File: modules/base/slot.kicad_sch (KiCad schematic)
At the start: 8 parts, among them J7 Conn_01x02, U6 TPS2111APWR

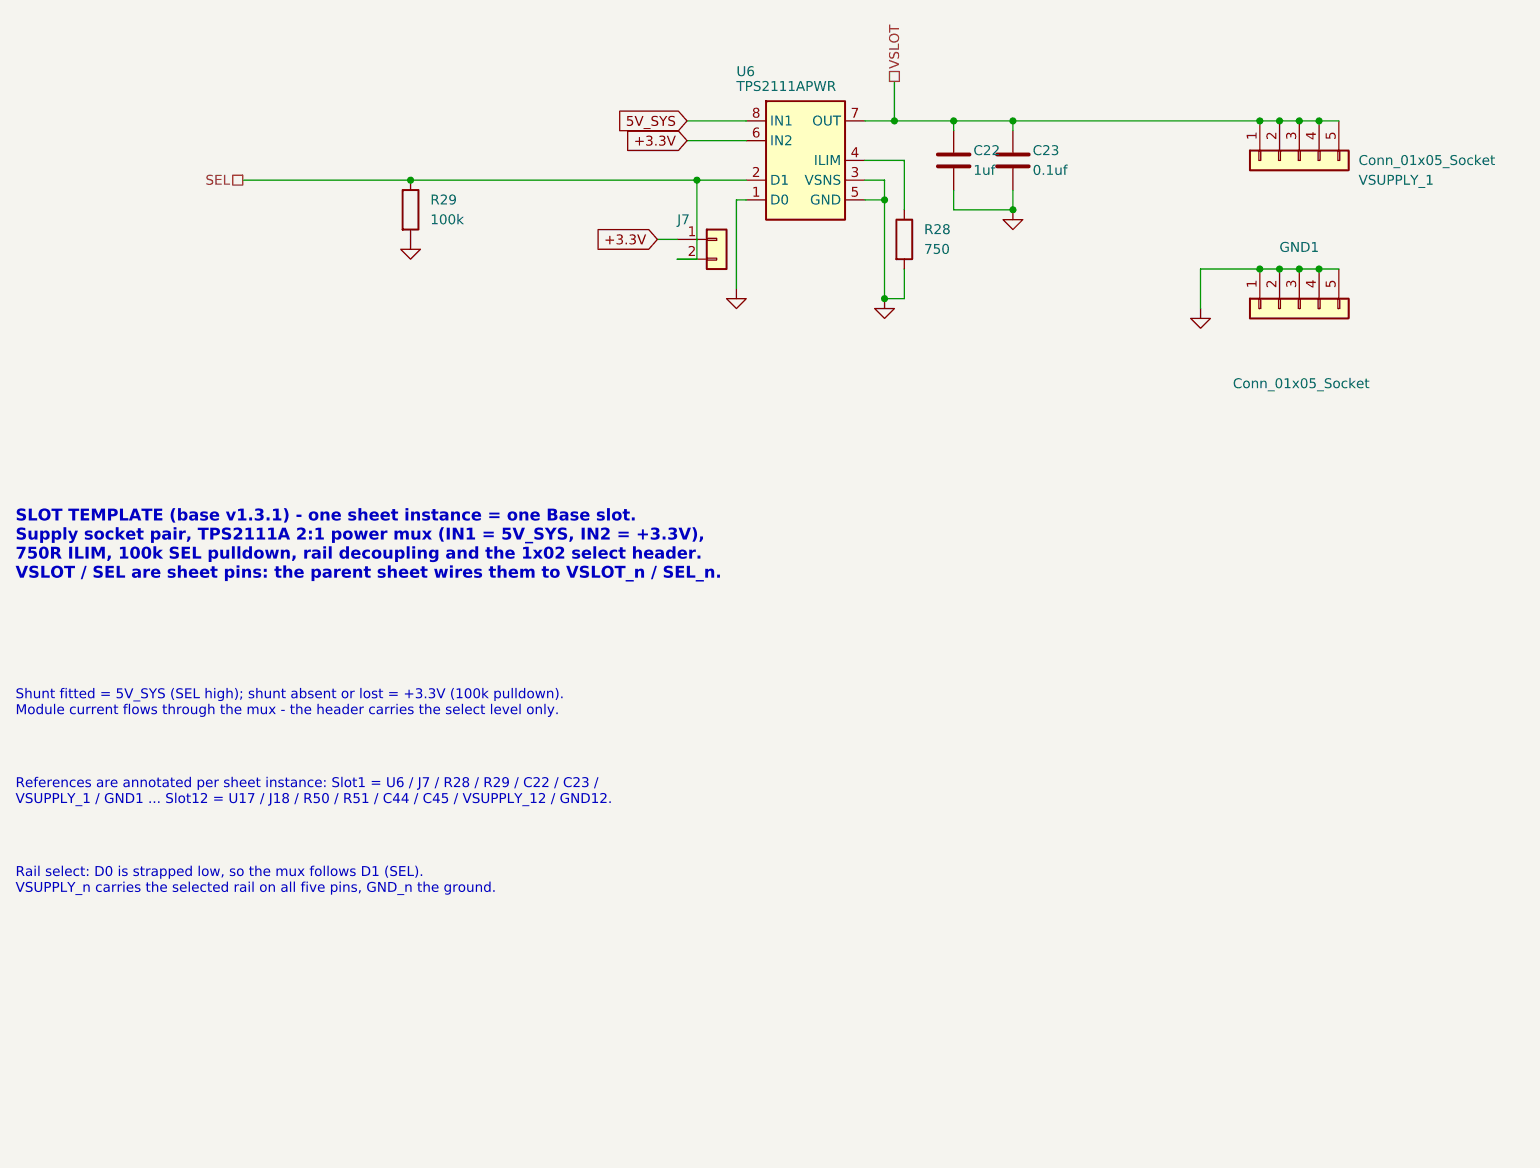
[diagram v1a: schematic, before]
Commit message: base: 1.3.8 (schematic only) - per-slot 2:1 mux swapped TPS2111APWR -> TPS2116DRLR (C3235557, ~$13/board cheaper), 12x 750R ILIM resistors deleted; docs/verification updated. NOTE: documented release blocker (reset press can drive a 3.3V-jumpered slot to 5V_SYS) + ILIM limit lost; PCB pending
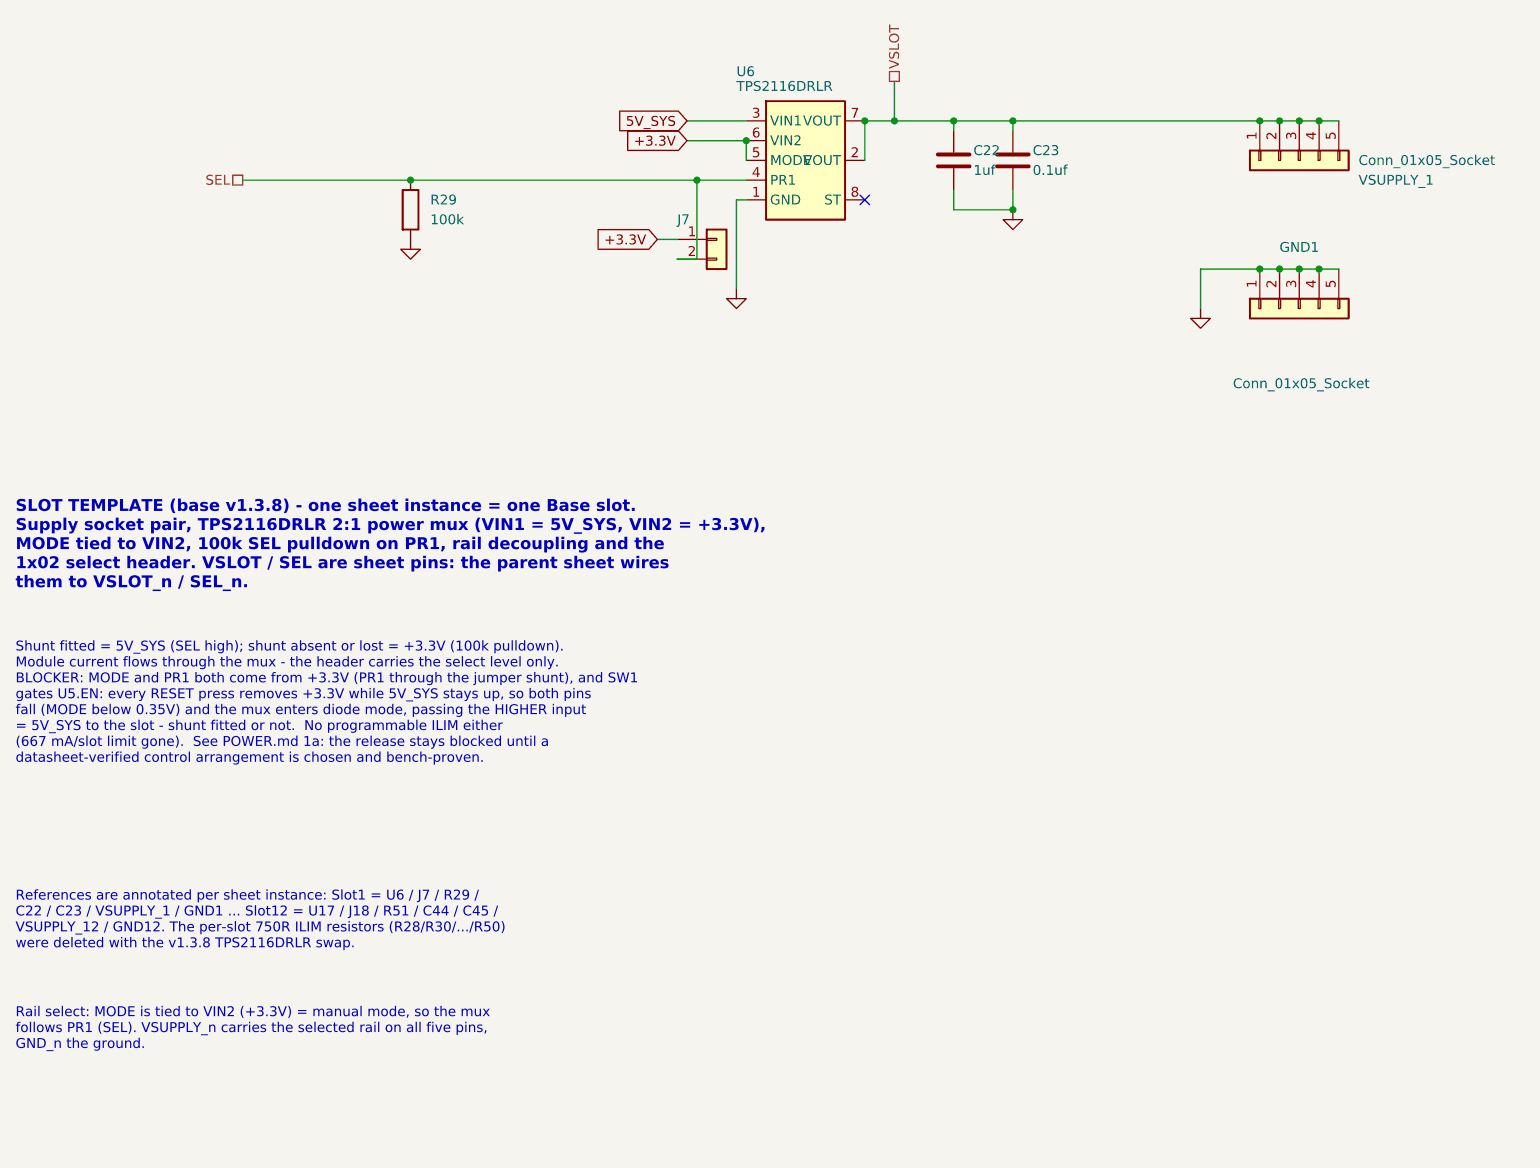
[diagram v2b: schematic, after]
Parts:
- removed R28: 750, Resistor_SMD:R_0402_1005Metric, symbol Device:R
- U6: value TPS2111APWR -> TPS2116DRLR; footprint Package_SO:TSSOP-8_4.4x3mm_P0.65mm -> Package_TO_SOT_SMD:SOT-583-8; symbol BreadModular_PowerMux:TPS2111APWR -> BreadModular_PowerMux:TPS2116DRLR; LCSC C471060 -> C3235557; MPN TPS2111APWR -> TPS2116DRLR
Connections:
- net +3.3V: now also U6.5 (MODE)
- net 5V_SYS: now also U6.3 (VIN1); no longer U6.8 (IN1)
- net GND: no longer U6.3 (VSNS), U6.5 (GND)
- net SEL: now also U6.4 (PR1); no longer U6.2 (D1)
- net VSLOT: now also U6.2 (VOUT)
- no-connect marks 0 -> 1
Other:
- note added: "Rail select: MODE is tied to VIN2 (+3.3V) = manual mode, so the mux follows PR1 (SEL). VSUPPLY_n carries the selected rail on all five pins, GND_n the ground."
- note added: "References are annotated per sheet instance: Slot1 = U6 / J7 / R29 / C22 / C23 / VSUPPLY_1 / GND1 ... Slot12 = U17 / J18 / R51 / C44 / C45 / VSUPPLY_12 / GND12. The per-slot 750R ILIM resistors (R28/R30/.../R50) were deleted with the v1.3.8 TPS2116DRLR swap."
- note added: "SLOT TEMPLATE (base v1.3.8) - one sheet instance = one Base slot. Supply socket pair, TPS2116DRLR 2:1 power mux (VIN1 = 5V_SYS, VIN2 = +3.3V), MODE tied to VIN2, 100k SEL pulldown on PR1, rail decoupling and the 1x02 select header. VSLOT / SEL are sheet pins: the parent sheet wires them to VSLOT_n / SEL_n."
- note added: "Shunt fitted = 5V_SYS (SEL high); shunt absent or lost = +3.3V (100k pulldown). Module current flows through the mux - the header carries the select level only. BLOCKER: MODE and PR1 both come from +3.3V (PR1 through the jumper shunt), and SW1 gates U5.EN: every RESET press removes +3.3V while 5V_SYS stays up, so both pins fall (MODE below 0.35V) and the mux enters diode mode, passing the HIGHER 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"
- note removed: "Rail select: D0 is strapped low, so the mux follows D1 (SEL). VSUPPLY_n carries the selected rail on all five pins, GND_n the ground."
- note removed: "References are annotated per sheet instance: Slot1 = U6 / J7 / R28 / R29 / C22 / C23 / VSUPPLY_1 / GND1 ... Slot12 = U17 / J18 / R50 / R51 / C44 / C45 / VSUPPLY_12 / GND12."
- note removed: "SLOT TEMPLATE (base v1.3.1) - one sheet instance = one Base slot. Supply socket pair, TPS2111A 2:1 power mux (IN1 = 5V_SYS, IN2 = +3.3V), 750R ILIM, 100k SEL pulldown, rail decoupling and the 1x02 select header. VSLOT / SEL are sheet pins: the parent sheet wires them to VSLOT_n / SEL_n."
- note removed: "Shunt fitted = 5V_SYS (SEL high); shunt absent or lost = +3.3V (100k pulldown). Module current flows through the mux - the header carries the select level only."

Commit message: base: 1.3.9 (schematic only) - per-slot mux select (MODE + J(n+6) pin 1) re-referenced +3.3V -> VBUS_PROT, resolving the 1.3.8 reset blocker
Blocker (v1.3.8): MODE was tied to VIN2 = +3.3V and PR1 was fed from the same rail
through the jumper shunt. SW1 gates U5.EN, so every RESET press removed +3.3V while
5V_SYS stayed up; both control pins fell (MODE < VIL,MODE = 0.35V, PR1 already
below VREF ~ 1V), the TPS2116DRLR entered diode mode and passed the HIGHER input -
a 3.3V-jumpered slot was fed 5V_SYS on every reset press, shunt fitted or absent.

Fix: MODE and the J(n+6) pin-1 reference move to VBUS_PROT (the always-on protected
5V upstream of F2); VIN2 stays +3.3V; jumper, 100k PR1 pulldown and every
SEL_n/VSLOT_n net name unchanged. Datasheet basis TI SLVSFG1A: Table 5-1 (MODE
"pulled up to an external voltage" = manual mode) + 7.6.1.2 ("GPIO can be directly
connected to PR1 when MODE is tied high (>=1V)"), 6.5 (VIH,MODE 1..5.5V, VIL,MODE
0..0.35V, VREF 0.92/1/1.08V), 6.3 (VST/VMODE/VPR1 = 0..5.5V independent of VINx)
and 6.1 (abs max -0.3..6V) - so ~5V on those pins is inside spec and no series or
divider resistor is required.

RESET/power-up: the select no longer follows the 3.3V rail down. On reset MODE stays
~5V = manual mode and PR1 low selects VIN2: a 3.3V-jumpered slot goes to 0V
(deselected), never 5V_SYS; a 5V-jumpered slot still gets 5V. The residual
diode-mode window needs MODE <= 0.35V, i.e. VBUS_PROT <= 0.35V, while both inputs
are derived from VBUS_PROT - so both are <= 0.35V and it cannot present 5V.

Only slot.kicad_sch changed (one template, all twelve U6..U17 / J7..J18), plus
POWER.md 1a/2/3.2/3.3, CHANGELOG, VERSION -> 1.3.9, the new deterministic tool and
its evidence. base.kicad_sch byte-identical, base.kicad_pcb byte-identical
(b8df0829...). ERC 11 before / 11 after, identical by identity. Accepted risk:
the 667 mA per-slot ILIM limit stays gone. PCB pending: 1.3.8 footprint/ILIM work
plus the new J7..J18 pin-1 net move.
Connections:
- net +3.3V: no longer J7.1 (Pin_1), U6.5 (MODE)
- new net VBUS_PROT: J7.1 (Pin_1), U6.5 (MODE)
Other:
- note added: "Rail select: MODE is pulled up to VBUS_PROT (external bias >= 1V) = manual mode, so the mux follows PR1 (SEL). VSUPPLY_n carries the selected rail on all five pins, GND_n the ground."
- note added: "SLOT TEMPLATE (base v1.3.9) - one sheet instance = one Base slot. Supply socket pair, TPS2116DRLR 2:1 power mux (VIN1 = 5V_SYS, VIN2 = +3.3V), MODE and the jumper pin-1 reference on VBUS_PROT (the select survives a reset), 100k SEL pulldown on PR1, rail decoupling and the 1x02 select header. VSLOT / SEL are sheet pins: the parent sheet wires them to VSLOT_n / SEL_n."
- note added: "Shunt fitted = 5V_SYS (SEL high, PR1 = VBUS_PROT); shunt absent or lost = +3.3V (SEL low, 100k pulldown). Module current flows through the mux - the header carries the select level only. v1.3.9: MODE and the jumper reference now come from VBUS_PROT, not +3.3V, so the select state no longer follows the 3.3V rail down. A RESET press leaves MODE >= 1V (manual mode) and PR1 low selects VIN2 = 0V: a 3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"
- note removed: "Rail select: MODE is tied to VIN2 (+3.3V) = manual mode, so the mux follows PR1 (SEL). VSUPPLY_n carries the selected rail on all five pins, GND_n the ground."
- note removed: "SLOT TEMPLATE (base v1.3.8) - one sheet instance = one Base slot. Supply socket pair, TPS2116DRLR 2:1 power mux (VIN1 = 5V_SYS, VIN2 = +3.3V), MODE tied to VIN2, 100k SEL pulldown on PR1, rail decoupling and the 1x02 select header. VSLOT / SEL are sheet pins: the parent sheet wires them to VSLOT_n / SEL_n."
- note removed: "Shunt fitted = 5V_SYS (SEL high); shunt absent or lost = +3.3V (100k pulldown). Module current flows through the mux - the header carries the select level only. BLOCKER: MODE and PR1 both come from +3.3V (PR1 through the jumper shunt), and SW1 gates U5.EN: every RESET press removes +3.3V while 5V_SYS stays up, so both pins fall (MODE below 0.35V) and the mux enters diode mode, passing the HIGHER 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"
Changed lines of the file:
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@@
 	(generator_version "10.0")
 	(paper "A4")
-	(text "SLOT TEMPLATE (base v1.3.8) - one sheet instance = one Base slot.\nSupply socket pair, TPS2116DRLR 2:1 power mux (VIN1 = 5V_SYS, VIN2 = +3.3V),\nMODE tied to VIN2, 100k SEL pulldown on PR1, rail decoupling and the\n1x02 select header. VSLOT / SEL are sheet pins: the parent sheet wires\nthem to VSLOT_n / SEL_n."
+	(text "SLOT TEMPLATE (base v1.3.9) - one sheet instance = one Base slot.\nSupply socket pair, TPS2116DRLR 2:1 power mux (VIN1 = 5V_SYS, VIN2 = +3.3V),\nMODE and the jumper pin-1 reference on VBUS_PROT (the select survives a reset),\n100k SEL pulldown on PR1, rail decoupling and the 1x02 select header. VSLOT /\nSEL are sheet pins: the parent sheet wires them to VSLOT_n / SEL_n."
 		(exclude_from_sim no)
 		(at 25.4 96.52 0)
@@
 		)
 	)
-	(text "Rail select: MODE is tied to VIN2 (+3.3V) = manual mode, so the mux\nfollows PR1 (SEL). VSUPPLY_n carries the selected rail on all five pins,\nGND_n the ground."
+	(text "Rail select: MODE is pulled up to VBUS_PROT (external bias >= 1V) = manual\nmode, so the mux follows PR1 (SEL). VSUPPLY_n carries the selected rail on all\nfive pins, GND_n the ground."
 		(exclude_from_sim no)
 		(at 25.4 158.75 0)
@@
 		)
 	)
-	(text "Shunt fitted = 5V_SYS (SEL high); shunt absent or lost = +3.3V (100k pulldown).\nModule current flows through the mux - the header carries the select level only.\nBLOCKER: MODE and PR1 both come from +3.3V (PR1 through the jumper shunt), and SW1\ngates U5.EN: every RESET press removes +3.3V while 5V_SYS stays up, so both pins\nfall (MODE below 0.35V) and the mux enters diode mode, passing the HIGHER input\n= 5V_SYS to the slot - shunt fitted or not.  No programmable ILIM either\n(667 mA/slot limit gone).  See POWER.md 1a: the release stays blocked until a\ndatasheet-verified control arrangement is chosen and bench-proven."
+	(text "Shunt fitted = 5V_SYS (SEL high, PR1 = VBUS_PROT); shunt absent or lost = +3.3V\n(SEL low, 100k pulldown). Module current flows through the mux - the header\ncarries the select level only. v1.3.9: MODE and the jumper reference now come\nfrom VBUS_PROT, not +3.3V, so the select state no longer follows the 3.3V rail\ndown. A RESET press leaves MODE >= 1V (manual mode) and PR1 low selects\nVIN2 = 0V: a 3.3V-jumpered slot is deselected, never driven to 5V_SYS. The mux\nhas no programmable ILIM (the 667 mA/slot limit is gone). See POWER.md 1a."
 		(exclude_from_sim no)
 		(at 25.4 116.84 0)
@@
 	(wire
 		(pts
-			(xy 119.38 44.45) (xy 119.38 46.99)
-		)
-		(stroke
-			(width 0)
-			(type default)
-		)
-	)
-	(wire
-		(pts
 			(xy 134.62 41.91) (xy 134.62 46.99)
 		)
@@
 			(type default)
 		)
-	)
-	(junction
-		(at 119.38 44.45)
-		(diameter 0)
-		(color 0 0 0 0)
 	)
 	(junction
@@
 			(width 0)
 			(type default)
+		)
+	)
+	(wire
+		(pts
+			(xy 111.76 46.99) (xy 119.38 46.99)
+		)
+		(stroke
+			(width 0)
+			(type default)
+		)
+	)
+	(global_label "VBUS_PROT"
+		(shape input)
+		(at 111.76 46.99 180)
+		(fields_autoplaced yes)
+		(effects
+			(font
+				(size 1.27 1.27)
+			)
+			(justify right)
+		)
+		(property "Intersheetrefs" "${INTERSHEET_REFS}"
+			(at 111.76 46.99 180)
+			(hide yes)
+			(show_name no)
+			(do_not_autoplace no)
+			(effects
+				(font
+					(size 1.27 1.27)
+				)
+			)
 		)
 	)
@@
 		)
 	)
-	(global_label "+3.3V"
+	(global_label "VBUS_PROT"
 		(shape input)
 		(at 107.95 57.15 180)
@@
 			)
 		)
-		(property "Description" "Slot rail select header: pin1=+3.3V, pin2=SEL_n. Shunt fitted = 5V_SYS, open = +3.3V (100k pulldown). Logic only, no module current."
+		(property "Description" "Slot rail select header: pin1=VBUS_PROT (reset-surviving select reference), pin2=SEL_n. Shunt fitted = 5V_SYS, open = +3.3V (100k pulldown). Logic only, no module current."
 			(at 115.57 57.15 0)
 			(hide yes)
@@
 			)
 		)
-		(property "Description" "Per-slot 2:1 power mux (TPS2116DRLR): VIN1=5V_SYS, VIN2=+3.3V, MODE tied to VIN2 = manual mode, PR1=SEL_n (shunt = 5V_SYS, absent = +3.3V via 100k pulldown), VOUT on pins 2 and 7, ST not connected"
+		(property "Description" "Per-slot 2:1 power mux (TPS2116DRLR): VIN1=5V_SYS, VIN2=+3.3V, MODE pulled up to VBUS_PROT (>=1V external bias) = manual mode (v1.3.9: select reference no longer depends on +3.3V), PR1=SEL_n (shunt = VBUS_PROT -> VIN1 = 5V_SYS, absent = 100k pulldown -> VIN2 = +3.3V), VOUT on pins 2 and 7, ST not connected"
 			(at 127 46.99 0)
 			(hide yes)

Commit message: Update the base to 2.0.1
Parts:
- removed J7: Conn_01x02, Connector_PinHeader_2.00mm:PinHeader_1x02_P2.00mm_Vertical, symbol Connector_Generic:Conn_01x02
- added D4: LED, LED_SMD:LED_0603_1608Metric, symbol BreadModular_Selectors:Indicator_LED
- added Q1: AO3400A, Package_TO_SOT_SMD:SOT-23, symbol Transistor_FET:Q_NMOS_GSD
- added R62: 1k, Resistor_SMD:R_0402_1005Metric, symbol Device:R
- added SW2: MSK12C02, BreadModular_Selectors:SW_SPDT_Shouhan_MSK12C02_C431540, symbol BreadModular_Selectors:MSK12C02
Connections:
- net 5V_SYS: now also R62.1
- net GND: now also Q1.2 (S), SW2.4 (SHIELD)
- net SEL: now also Q1.1 (G), SW2.2 (B)
- net VBUS_PROT: now also SW2.3 (C)
- new net LED_A: D4.2 (A), R62.2
- new net LED_K: D4.1 (K), Q1.3 (D)
- no-connect marks 1 -> 2
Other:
- note added: "5V position: SW pin 2 connects to pin 3 (VBUS_PROT); SEL high selects 5V_SYS. 3V3 position: SW pin 2 connects to unused pin 1; the retained 100k resistor pulls SEL low and selects +3.3V. Q drives the LED without loading SEL. The LED supply is 5V_SYS. RESET pulls the 3.3V rail low, not SEL or MODE; a 3V3-selected slot is not switched to 5V by pressing RESET."
- note added: "Per-instance refs: Slot1 = U6 / SW2 / Q1 / D4 / R62 / R29 / C22 / C23. Slot12 = U17 / SW13 / Q12 / D15 / R73 / R51 / C44 / C45. VSUPPLY_1..12 and GND1..12 remain the mating sockets. J7..J18 shunt jumpers were replaced by SW2..SW13."
- note added: "Rail select uses manual mode (MODE = VBUS_PROT). VSUPPLY_n carries the selected rail on all five pins; GND_n carries ground on all five pins. No programmable per-slot current limit. See POWER.md for system limits."
- note added: "SLOT TEMPLATE - SMD rail selector and buffered 5V indicator. TPS2116DRLR: VIN1 = 5V_SYS, VIN2 = +3.3V; MODE = VBUS_PROT. SEL / VSLOT are sheet pins connected to SEL_n / VSLOT_n in the parent. The switch carries logic only; module current flows through the power mux."
- note removed: "Rail select: MODE is pulled up to VBUS_PROT (external bias >= 1V) = manual mode, so the mux follows PR1 (SEL). VSUPPLY_n carries the selected rail on all five pins, GND_n the ground."
- note removed: "References are annotated per sheet instance: Slot1 = U6 / J7 / R29 / C22 / C23 / VSUPPLY_1 / GND1 ... Slot12 = U17 / J18 / R51 / C44 / C45 / VSUPPLY_12 / GND12. The per-slot 750R ILIM resistors (R28/R30/.../R50) were deleted with the v1.3.8 TPS2116DRLR swap."
- note removed: "SLOT TEMPLATE (base v1.3.9) - one sheet instance = one Base slot. Supply socket pair, TPS2116DRLR 2:1 power mux (VIN1 = 5V_SYS, VIN2 = +3.3V), MODE and the jumper pin-1 reference on VBUS_PROT (the select survives a reset), 100k SEL pulldown on PR1, rail decoupling and the 1x02 select header. VSLOT / SEL are sheet pins: the parent sheet wires them to VSLOT_n / SEL_n."
- note removed: "Shunt fitted = 5V_SYS (SEL high, PR1 = VBUS_PROT); shunt absent or lost = +3.3V (SEL low, 100k pulldown). Module current flows through the mux - the header carries the select level only. v1.3.9: MODE and the jumper reference now come from VBUS_PROT, not +3.3V, so the select state no longer follows the 3.3V rail down. A RESET press leaves MODE >= 1V (manual mode) and PR1 low selects VIN2 = 0V: a 3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"
